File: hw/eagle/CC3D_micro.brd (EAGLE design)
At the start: 29.7 x 19.3 mm, 76 parts, among them IC1 STM32F103CBT6, IC2 MPU-6050, IC3 MS5611, IC4 SPI_FLASH-X25XXSMD, IC5 MCP1703CB, U2 STM32F030XTSSOP20, Y1 8MHZ

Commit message: hw v0.2
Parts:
- removed C20: 47n, RC.v2:0402
- added C1: u47, RC.v2:0402
- added R1: 22, RC.v2:0402
- C10: value 47n -> u1
- C11, C3: value 0u1 -> 47n
- C12: device RC.v2:0603 -> RC.v2:0402
- C13, C14: value 2u2 -> 0u1; device RC.v2:0805 -> RC.v2:0402
- C16: value 47n -> 0u1; device RC.v2:0402 -> RC.v2:0603
- C17: value 2n2 50v -> 0u1
- C18: value u47 -> 2u2; device RC.v2:0402 -> RC.v2:0805
- C19: value u47 -> 2u2
- C2: value 0u1 -> u47
- C5: value 0u1 -> 2n2 50v
- C6: value u1 -> 47n
- C7: value u1 -> u47; device RC.v2:0402 -> RC.v2:0805
- C9: value u47 -> u1
- IC1: value STM32F103CBT6 -> MPU-6050; device cc3d:LQFP48 -> cc3d:QFN-24-TESTING
- IC2: value MPU-6050 -> MS5611; device cc3d:QFN-24-TESTING -> cc3d:LGA8
- IC3: value MS5611 -> MCP1703CB; device cc3d:LGA8 -> semi:SOT23
- IC4: value SPI_FLASH-X25XXSMD -> STM32F103CBT6; device cc3d:SO08 -> cc3d:LQFP48
- IC5: value MCP1703CB -> SPI_FLASH-X25XXSMD; device semi:SOT23 -> cc3d:SO08
- IC6: value STM32F030XTSSOP20 -> STM32F030F4T6
- PAD1: value (none) -> VCC
- PAD10, PAD16: value SWCLK -> (none)
- PAD11: value PPM -> (none)
- PAD12: value RX/SDA -> (none)
- PAD13: value TX/SCL -> (none)
- PAD14: value VCC -> (none)
- PAD15: value GND -> (none)
- PAD17: value SWDIO -> (none)
- PAD2: value (none) -> GND
- PAD3: value (none) -> RX/SDA
- PAD4: value (none) -> TX/SCL
- PAD5, PAD8: value (none) -> SWCLK
- PAD6: value (none) -> SWDIO
- PAD7: value (none) -> PPM
- R10: value 10k -> 1k
- R11: value 15k -> 680
- R12: value 1k -> 510
- R14: value 510 -> 10k
- R15: value 680 -> 1k
- R16: value DNP -> 680
- R2: value 10k -> 22
- R3: value 10k -> 1k5
- R5: value 2k2 -> 10k
- R6: value 680 -> 2k2
- R7: value 22 -> 10k
- R8: value 22 -> 15k
- R9: value 1k5 -> DNP
- moved IC3 21.2 mm to (9.91, 3.68), flipped to the top, turned to 180 degrees
- moved R5 20.8 mm to (7.24, 16.3), turned to 0 degrees
- moved PAD1 19.8 mm to (-13.5, 5.33), turned to 90 degrees
- moved PAD12 18.2 mm to (3.17, 1.14), flipped to the top
- moved PAD15 17.6 mm to (3.17, 1.14), turned to 0 degrees
- moved PAD2 17.6 mm to (-13.5, 6.99), turned to 90 degrees
- moved PAD8 16.7 mm to (-6.22, 14.9)
- moved C7 16.6 mm to (9.78, 6.22), flipped to the top, turned to 180 degrees
- moved IC2 15.9 mm to (-10.8, 8.26)
- moved IC5 15.8 mm to (-4.83, 9.53)
- moved C18 15.7 mm to (-11.0, 2.67)
- moved R6 14.8 mm to (-12.4, 9.53), turned to 180 degrees
- moved PAD10 14.1 mm to (-3.17, 1.14), turned to 180 degrees
- moved PAD13 13.8 mm to (-3.17, 1.14), turned to 180 degrees
- moved R11 13.2 mm to (-4.52, 7.62), turned to 270 degrees
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- renumbered D5 to D1, U2 to IC6
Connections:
- new net N$7: IC6.1, R10.P$1
- net BAT: now also C18.P$2, C19.P$2, PAD10.1, PAD12.1, PAD14.1, PAD16.1; no longer C13.P$2, C14.P$2, PAD3.1, PAD4.1, PAD7.1, PAD8.1
- net FLEXI_RX/SDA: now also IC2.7, IC4.22, PAD3.1, R6.P$1; no longer IC1.22, IC3.7, PAD12.1, R5.P$1
- net FLEXI_TX/SCL: now also IC2.8, IC4.21, PAD4.1; no longer IC1.21, IC3.8, PAD13.1
- net GND: now also C1.P$1, C10.P$2, C11.P$1, C12.P$1, C16.P$2, C17.P$2, C7.P$1, IC1.1, IC1.11, IC1.18, IC2.3, IC2.4, IC3.1, IC4.23, IC4.35, IC4.47, IC4.8, IC5.4, PAD2.1, R10.P$2, R15.P$2, R8.P$2; no longer C10.P$1, C11.P$2, C12.P$2, C16.P$1, C17.P$1, C20.P$1, C7.P$2, IC1.23, IC1.35, IC1.47, IC1.8, IC2.1, IC2.11, IC2.18, IC3.3, IC3.4, IC4.4, IC5.1, IC6.1, PAD15.1, R11.P$2, R12.P$2
- net M1+: now also PAD11.1; no longer PAD1.1
- net M2+: now also PAD15.1, Q3.1; no longer PAD2.1, Q2.1
- net M3+: now also PAD13.1, Q2.1; no longer PAD5.1, Q3.1
- net M4+: now also PAD17.1; no longer PAD6.1
- net MAIN_RX: now also IC4.31; no longer IC1.31
- net MAIN_TX: now also IC4.30, R12.P$2; no longer IC1.30, R14.P$2
- net N$1: now also IC1.12, IC4.13, R9.P$1; no longer IC1.13, IC2.12, R16.P$1
- net N$10: now also IC4.26, IC5.6; no longer IC1.26, IC4.6
- net N$11: now also IC4.27, IC5.2; no longer IC1.27, IC4.2
- net N$12: now also IC4.28, IC5.5; no longer IC1.28, IC4.5
- net N$13: now also IC4.6; no longer IC1.6
- net N$15: now also IC4.39, R16.P$1; no longer IC1.39, R6.P$1
- net N$16: now also R16.P$2; no longer R6.P$2
- net N$17: now also IC4.3, R7.P$2, R8.P$1; no longer IC1.3, R10.P$2, R11.P$1
- net N$18: now also R2.P$2; no longer R8.P$2
- net N$19: now also IC4.44, R15.P$1; no longer IC1.44, R12.P$1
- net N$2: now also IC1.8, IC4.14, R5.P$1; no longer IC1.14, IC2.8, R2.P$1
- net N$20: now also R1.P$2; no longer R7.P$2
- net N$24: now also R11.P$2; no longer R15.P$2
- net N$25: now also IC6.12
- net N$27: now also R12.P$1; no longer R14.P$1
- net N$3: now also IC1.23, IC4.15; no longer IC1.15, IC2.23
- net N$30: now also PAD8.1; no longer PAD10.1
- net N$31: now also R11.P$1; no longer R15.P$1
- net N$32: now also C4.P$2, IC1.10; no longer C15.P$2, IC2.10
- net N$33: now also IC4.5; no longer IC1.5
- net N$34: now also C5.P$2, IC1.20; no longer C17.P$2, IC2.20
- net N$35: now also IC4.11, PAD7.1; no longer IC1.11, PAD11.1
- net N$36: now also IC3.3; no longer IC5.3
- net N$37: now also C8.P$2, IC4.7; no longer C20.P$2, IC1.7
- net N$38: now also C11.P$2; no longer C8.P$2
- net N$4: now also IC1.9, IC4.16; no longer IC1.16, IC2.9
- net N$5: now also IC1.24, IC4.17; no longer IC1.17, IC2.24
- net N$6: now also IC4.10; no longer IC1.10
- net N$9: now also IC4.25, IC5.1, R14.P$1; no longer IC1.25, IC4.1, R3.P$1
- net PWM1: now also IC4.46; no longer IC1.46
- net PWM2: now also IC4.45, Q3.3, R19.P$2; no longer IC1.45, Q2.3, R18.P$2
- net PWM3: now also IC4.43, Q2.3, R18.P$2; no longer IC1.43, Q3.3, R19.P$2
- net PWM4: now also IC4.29; no longer IC1.29
- net SWCLK: now also IC4.37, PAD5.1; no longer IC1.37, PAD16.1
- net SWDIO: now also IC4.34, PAD6.1; no longer IC1.34, PAD17.1
- net USB_DM: now also IC4.32, R2.P$1; no longer IC1.32, R8.P$1
- net USB_DP: now also IC4.33, R1.P$1, R3.P$2; no longer IC1.33, R7.P$1, R9.P$2
- net VBUS: now also R7.P$1; no longer R10.P$1
- net VCC: now also C10.P$1, C12.P$2, C13.P$2, C14.P$2, C15.P$2, C16.P$1, C17.P$1, C7.P$2, C9.P$2, IC3.2, IC4.1, IC4.24, IC4.36, IC4.48, IC4.9, IC5.3, IC5.7, IC5.8, PAD1.1, R14.P$2, R3.P$1, R6.P$2, R9.P$2; no longer C11.P$1, C12.P$1, C19.P$2, C2.P$2, C3.P$2, C4.P$2, C5.P$2, C6.P$2, C7.P$1, IC1.1, IC1.24, IC1.36, IC1.48, IC1.9, IC4.3, IC4.7, IC4.8, IC5.2, PAD14.1, R16.P$2, R2.P$2, R3.P$2, R9.P$1
- net V_BARO: now also C1.P$2, C6.P$2, IC2.1, IC2.2; no longer C10.P$2, C9.P$2, IC3.1, IC3.2
- net V_GYRO: now also C2.P$2, C3.P$2, IC1.13; no longer C16.P$2, C18.P$2, IC2.13
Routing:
- net GND: track 139.9 -> 137.9 mm
- net N$7: track 0.00 -> 1.07 mm
- net N$25: track 5.11 -> 5.93 mm
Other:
- board text added: "BIND"
- board text added: "V0.2"

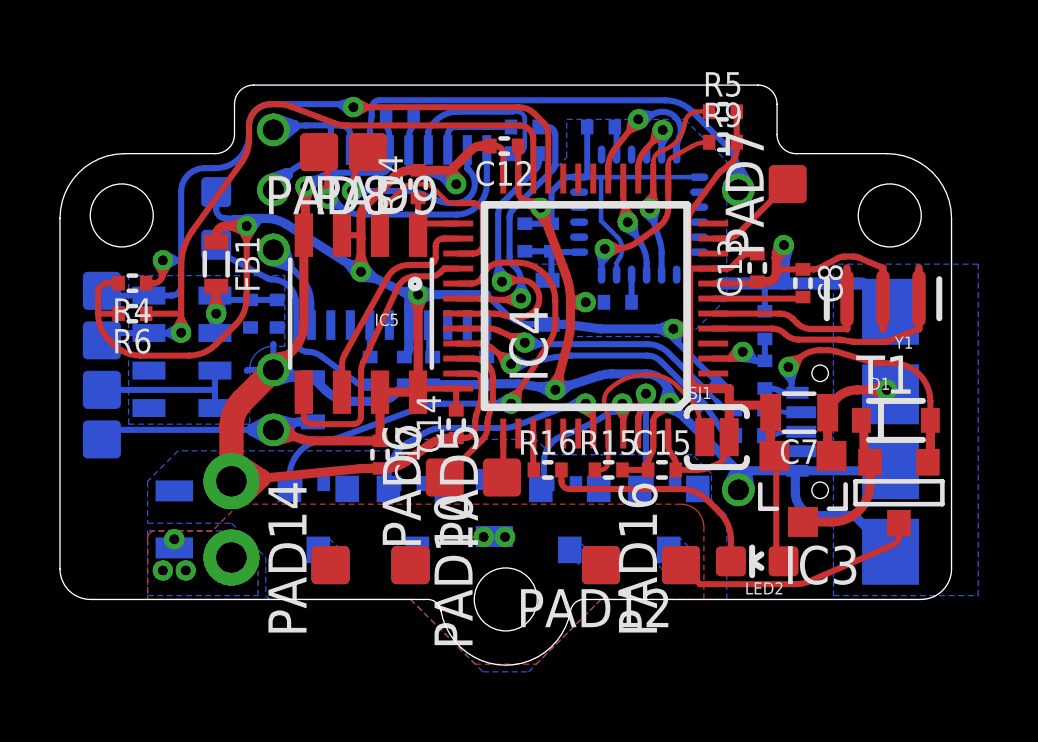
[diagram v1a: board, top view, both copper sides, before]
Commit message: add BOM
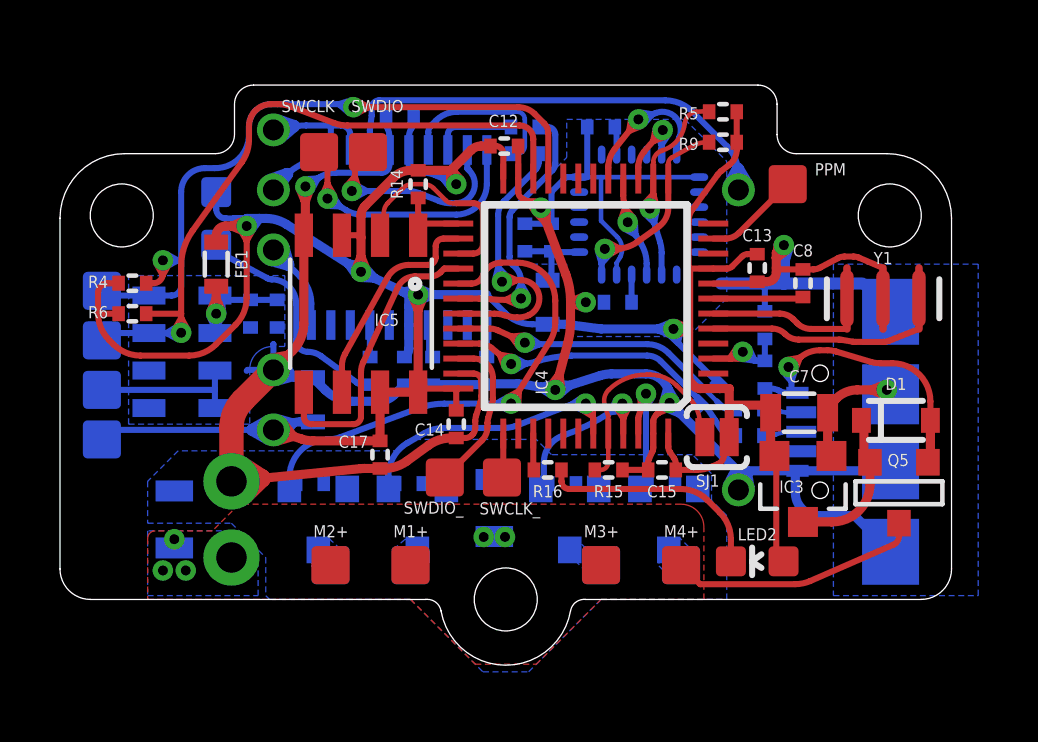
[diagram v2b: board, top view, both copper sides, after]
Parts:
- removed PAD10, PAD11, PAD12, PAD13, PAD14, PAD15, PAD16, PAD17: (no value), cc3d:SMD1,27-2,54
- added M1+, M1-, M2+, M2-, M3+, M3-, M4+, M4-: (no value), cc3d:SMD1,27-2,54
- 3V3: value VCC -> (none)
- D1: value (none) -> BAT54
- GND: value GND -> (none)
- IC1: value MPU-6050 -> MPU-6000
- IC3: value MCP1703CB -> XC6206P332
- IC5: value SPI_FLASH-X25XXSMD -> M25P16
- JP1: value M021X02_NO_SILK -> BAT
- PPM: value PPM -> (none)
- Q1, Q2, Q3, Q4: value (none) -> Si2312
- Q5: value (none) -> AO3401
- RX/SDA: value RX/SDA -> (none)
- SJ1: value JUMPER-PAD-2-NC_BY_PASTE -> BOOT
- SWCLK, SWCLK_: value SWCLK -> (none)
- SWDIO, SWDIO_: value SWDIO -> (none)
- TX/SCL: value TX/SCL -> (none)
- U$1: value UNTITLED_USB_AB -> microUSB
- renumbered PAD1 to 3V3, PAD2 to GND, PAD3 to RX/SDA, PAD4 to TX/SCL, PAD5 to SWCLK_, PAD6 to SWDIO_, PAD7 to PPM, PAD8 to SWCLK, PAD9 to SWDIO, T1 to Q5
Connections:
- net BAT: now also M1+.1, M2+.1, M3+.1, M4+.1; no longer PAD10.1, PAD12.1, PAD14.1, PAD16.1
- net M1+: now also M1-.1; no longer PAD11.1
- net M2+: now also M2-.1; no longer PAD15.1
- net M3+: now also M3-.1; no longer PAD13.1
- net M4+: now also M4-.1; no longer PAD17.1
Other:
- board text added: "0u1"
- board text added: "10k"
- board text added: "15k"
- board text added: "1k"
- board text added: "1k5"
- board text added: "22"
- board text added: "2k2"
- board text added: "2n2 50v"
- board text added: "2u2"
- board text added: "3V3"
- board text added: "47n"
- board text added: "510"
- board text added: "680"
- board text added: "8MHZ"
- board text added: "AO3401"
- board text added: "BAT"
- board text added: "BAT54"
- board text added: "BOOT"
- board text added: "C1"
- board text added: "C10"
- board text added: "C11"
- board text added: "C12"
- board text added: "C13"
- board text added: "C14"
- board text added: "C15"
- board text added: "C16"
- board text added: "C17"
- board text added: "C18"
- board text added: "C19"
- board text added: "C2"
- board text added: "C3"
- board text added: "C4"
- board text added: "C5"
- board text added: "C6"
- board text added: "C7"
- board text added: "C8"
- board text added: "C9"
- board text added: "D1"
- board text added: "DNP"
- board text added: "FB1"
- board text added: "FB2"
- board text added: "GND"
- board text added: "IC1"
- board text added: "IC2"
- board text added: "IC3"
- board text added: "IC4"
- board text added: "IC5"
- board text added: "IC6"
- board text added: "JP1"
- board text added: "LED1"
- board text added: "LED2"
- board text added: "M1+"
- board text added: "M1-"
- board text added: "M2+"
- board text added: "M2-"
- board text added: "M25P16"
- board text added: "M3+"
- board text added: "M3-"
- board text added: "M4+"
- board text added: "M4-"
- board text added: "MS5611"
- board text added: "Q1"
- board text added: "Q2"
- board text added: "Q3"
- board text added: "Q4"
- board text added: "Q5"
- board text added: "R1"
- board text added: "R10"
- board text added: "R11"
- board text added: "R12"
- board text added: "R13"
- board text added: "R14"
- board text added: "R15"
- board text added: "R16"
- board text added: "R17"
- board text added: "R18"
- board text added: "R19"
- board text added: "R2"
- board text added: "R20"
- board text added: "R3"
- board text added: "R4"
- board text added: "R5"
- board text added: "R6"
- board text added: "R7"
- board text added: "R8"
- board text added: "R9"
- board text added: "RX/SDA"
- board text added: "SJ1"
- board text added: "STM32F030F4T6"
- board text added: "STM32F103CBT6"
- board text added: "SWCLK"
- board text added: "SWDIO"
- board text added: "Si2312"
- board text added: "TX/SCL"
- board text added: "U$1"
- board text added: "XC6206P332"
- board text added: "Y1"
- board text added: "microUSB"
- board text added: "u1"
- board text added: "u47"
- board text removed: "M1"
- board text removed: "M2"
- board text removed: "M3"
- board text removed: "M4"
